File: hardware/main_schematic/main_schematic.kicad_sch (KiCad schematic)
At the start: 0 parts

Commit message: kicad started
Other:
- added sheet Sensor based MCU (sensor-based-mcu.kicad_sch)
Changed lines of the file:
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@@
 	(generator_version "10.0")
 	(paper "A4")
+	(sheet
+		(at 49.53 62.23)
+		(size 30.48 25.4)
+		(exclude_from_sim no)
+		(in_bom yes)
+		(on_board yes)
+		(dnp no)
+		(fields_autoplaced yes)
+		(stroke
+			(width 0.1524)
+			(type solid)
+		)
+		(fill
+			(color 0 0 0 0)
+		)
+		(property "Sheetname" "Sensor based MCU"
+			(at 49.53 61.5184 0)
+			(show_name no)
+			(do_not_autoplace no)
+			(effects
+				(font
+					(size 1.27 1.27)
+				)
+				(justify left bottom)
+			)
+		)
+		(property "Sheetfile" "sensor-based-mcu.kicad_sch"
+			(at 49.53 88.2146 0)
+			(show_name no)
+			(do_not_autoplace no)
+			(effects
+				(font
+					(size 1.27 1.27)
+				)
+				(justify left top)
+			)
+		)
+		(instances
+			(project "main_schematic"
+				(path "/e5949f95-2d9e-4fb3-bbe4-3c2b333ddcca"
+					(page "2")
+				)
+			)
+		)
+	)
 	(sheet_instances
 		(path "/"

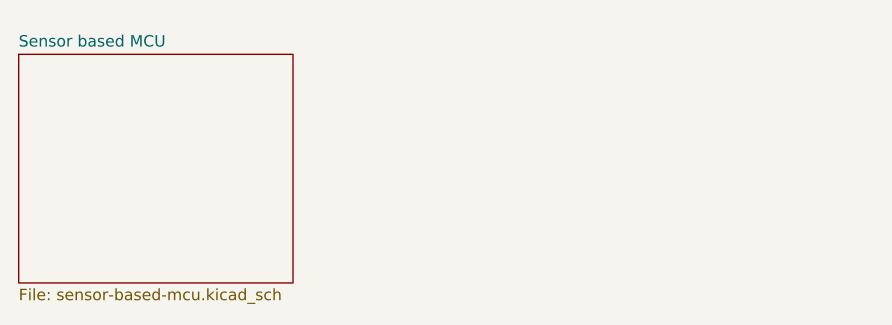
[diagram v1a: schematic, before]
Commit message: sensor based mcu
Schematic completed
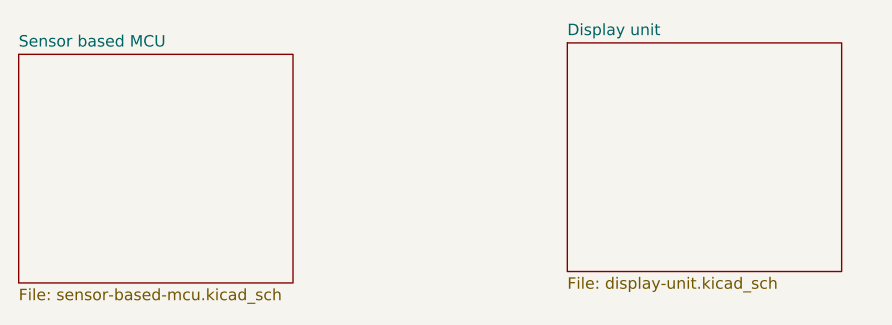
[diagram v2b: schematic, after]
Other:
- added sheet Display unit (display-unit.kicad_sch)
- company: (none) -> Marcel Siwiela
- title: (none) -> STM32 WIFI Project
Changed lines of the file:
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@@
 	(generator "eeschema")
 	(generator_version "10.0")
-	(paper "A4")
+	(paper "A5")
+	(title_block
+		(title "STM32 WIFI Project")
+		(date "2026-05-12")
+		(company "Marcel Siwiela")
+	)
+	(sheet
+		(at 110.49 60.96)
+		(size 30.48 25.4)
+		(exclude_from_sim no)
+		(in_bom yes)
+		(on_board yes)
+		(dnp no)
+		(fields_autoplaced yes)
+		(stroke
+			(width 0.1524)
+			(type solid)
+		)
+		(fill
+			(color 255 255 194 1)
+		)
+		(property "Sheetname" "Display unit"
+			(at 110.49 60.2484 0)
+			(show_name no)
+			(do_not_autoplace no)
+			(effects
+				(font
+					(size 1.27 1.27)
+				)
+				(justify left bottom)
+			)
+		)
+		(property "Sheetfile" "display-unit.kicad_sch"
+			(at 110.49 86.9446 0)
+			(show_name no)
+			(do_not_autoplace no)
+			(effects
+				(font
+					(size 1.27 1.27)
+				)
+				(justify left top)
+			)
+		)
+		(instances
+			(project "main_schematic"
+				(path "/e5949f95-2d9e-4fb3-bbe4-3c2b333ddcca"
+					(page "3")
+				)
+			)
+		)
+	)
 	(sheet
 		(at 49.53 62.23)
@@
 		)
 		(fill
-			(color 0 0 0 0)
+			(color 255 255 194 1)
 		)
 		(property "Sheetname" "Sensor based MCU"
